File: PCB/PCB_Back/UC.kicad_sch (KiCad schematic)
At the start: 39 parts, among them J1 Sensor connector, J2 USB_C_Receptacle_USB2.0, J3 Lipo connector, Q1 UMH3N, Q2 PMOS, SW1 SW_Push_Dual, U1 ESP-12E, U2 CH340C, U3 MCP73831-2-OT, U4 MCP1700x-330xxTT, U6 BME680

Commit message: Layout, Routing, Stuff
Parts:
- removed H4, H5: MountingHole, MountingHole:MountingHole_2.7mm_M2.5, symbol Mechanical:MountingHole
- added C24, C25: 100nF, Capacitor_SMD:C_0805_2012Metric, symbol Device:C
- R9: footprint Resistor_SMD:R_0815_2038Metric -> Resistor_SMD:R_0805_2012Metric
- U6: footprint KH-6X6X6H-STM:KH-6X6X6H-STM -> Package_LGA:Bosch_LGA-8_3x3mm_P0.8mm_ClockwisePinNumbering
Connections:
- net +3V3: now also C24.1, C25.1
- net GND: now also C24.2, C25.2
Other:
- company: (none) -> Waldo
- title: (none) -> Blahaj_Back

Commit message: Misc. Fixes, v1.0.
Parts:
- removed Q2: PMOS, Package_TO_SOT_SMD:SOT-23, symbol Simulation_SPICE:PMOS
- added Q3: Q_PMOS_GSD, Package_TO_SOT_SMD:SOT-23, symbol Device:Q_PMOS_GSD
- added SW2: SW_PWR, easyeda2kicad:SW-SMD_MK-12C02-G025, symbol Switch:SW_SPDT
- D16: footprint LED_SMD:LED_0805_2012Metric -> LED_SMD:LED_1206_3216Metric
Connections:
- net +5V: now also Q3.1 (G)
- net +BATT: now also Q3.3 (D)
- net VCC: now also SW2.2 (B); no longer C20.1, D17.1 (K)
- new net: C20.1, D17.1 (K), Q3.2 (S), SW2.3 (C)
- no-connect marks 17 -> 18
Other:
- moved on the sheet: C19, C20, D17, R13, U4

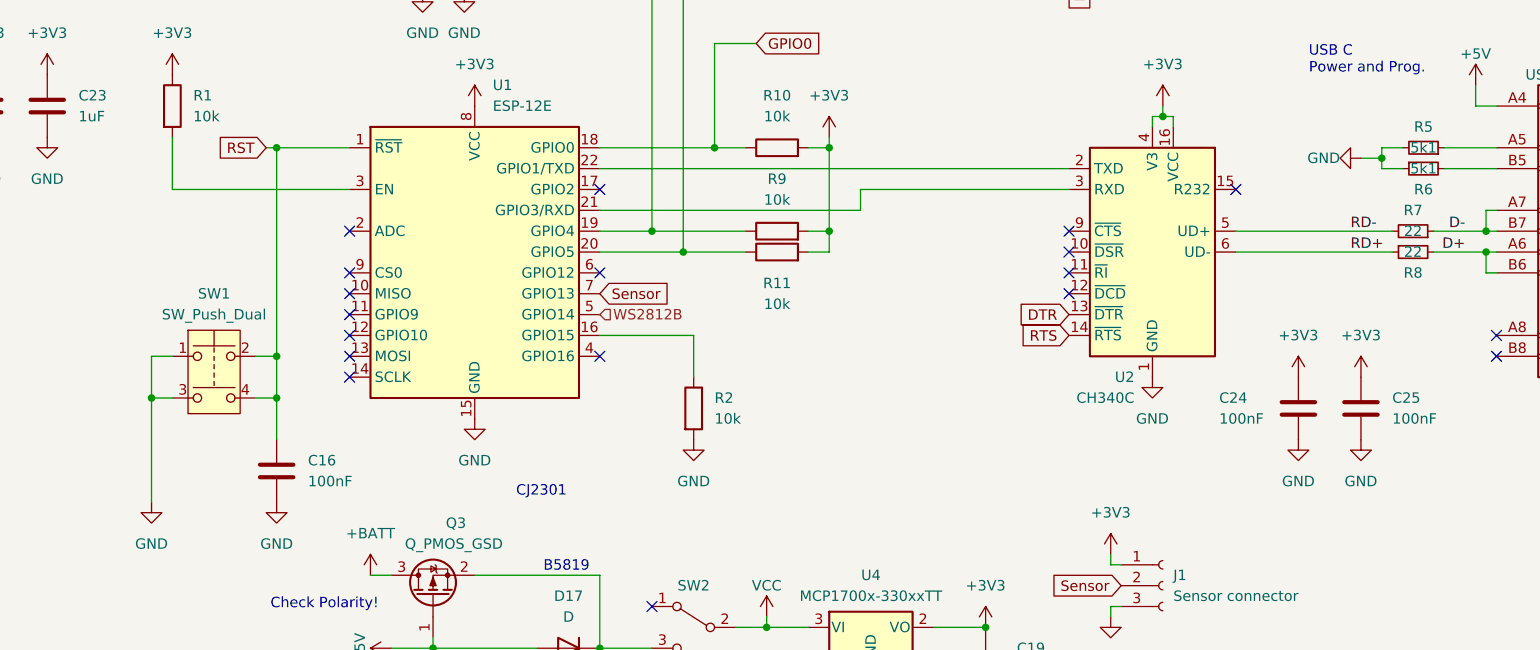
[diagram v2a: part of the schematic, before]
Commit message: Switched D+/D-, TX/RX, Switch Pins and rotated Lipo Marking
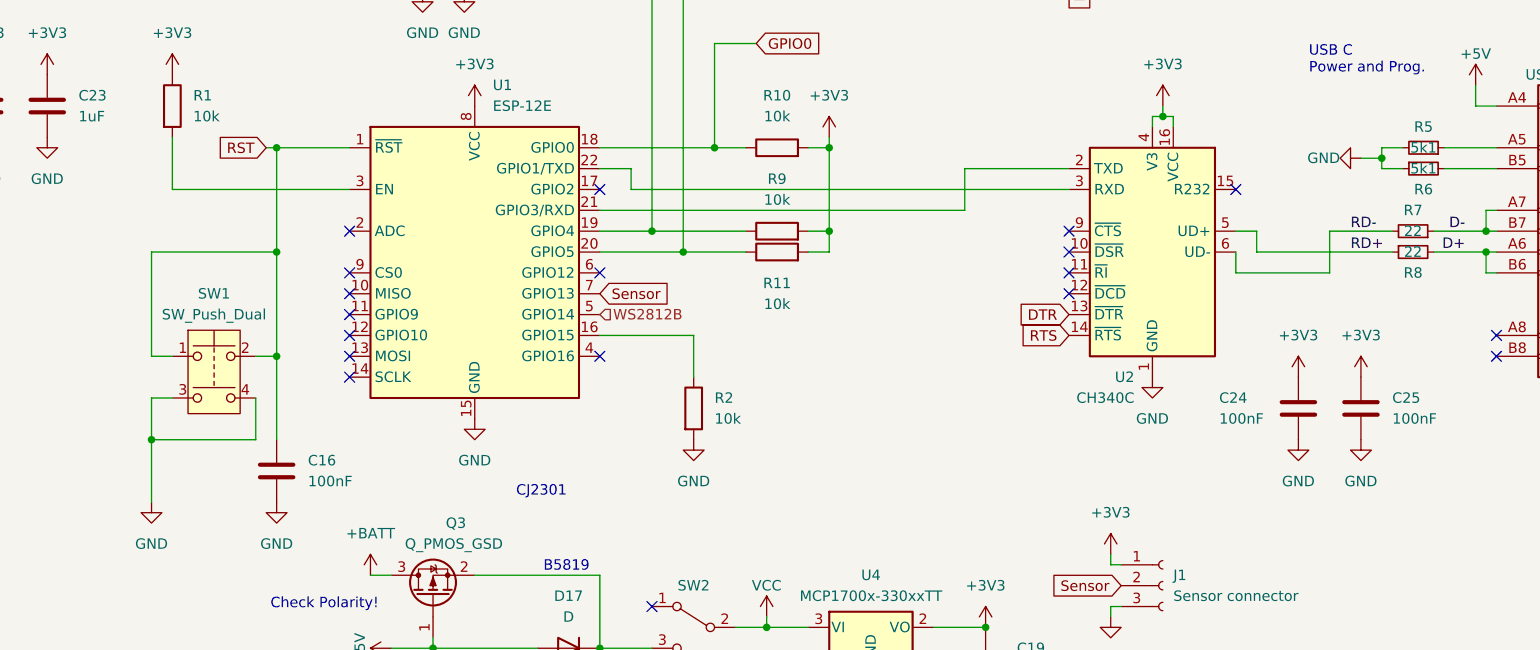
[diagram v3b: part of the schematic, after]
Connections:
- net GND: now also SW1.4; no longer SW1.1
- net RD+: now also U2.5 (UD+); no longer U2.6 (UD-)
- net RD-: now also U2.6 (UD-); no longer U2.5 (UD+)
- net RST: now also SW1.1; no longer SW1.4
- net at U1.21 (GPIO3/RXD): now also U2.2 (TXD); no longer U2.3 (RXD)
- net at U1.22 (GPIO1/TXD): now also U2.3 (RXD); no longer U2.2 (TXD)
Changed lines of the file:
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@@
-	)
-	(junction
-		(at 92.71 111.76)
-		(diameter 0)
-		(color 0 0 0 0)
-	)
-	(junction
-		(at 77.47 111.76)
-		(diameter 0)
-		(color 0 0 0 0)
 	)
 	(junction
@@
 	)
 	(junction
+		(at 77.47 116.84)
+		(diameter 0)
+		(color 0 0 0 0)
+	)
+	(junction
 		(at 256.54 115.57)
 		(diameter 0)
@@
 	)
 	(junction
+		(at 92.71 93.98)
+		(diameter 0)
+		(color 0 0 0 0)
+	)
+	(junction
 		(at 111.76 142.24)
 		(diameter 0)
@@
 	(wire
 		(pts
-			(xy 92.71 81.28) (xy 92.71 106.68)
+			(xy 92.71 81.28) (xy 92.71 93.98)
 		)
 		(stroke
@@
 	(wire
 		(pts
+			(xy 135.89 83.82) (xy 132.08 83.82)
+		)
+		(stroke
+			(width 0)
+			(type default)
+		)
+	)
+	(wire
+		(pts
 			(xy 143.51 104.14) (xy 132.08 104.14)
 		)
@@
 	(wire
 		(pts
+			(xy 189.23 86.36) (xy 135.89 86.36)
+		)
+		(stroke
+			(width 0)
+			(type default)
+		)
+	)
+	(wire
+		(pts
 			(xy 128.27 54.61) (xy 146.05 54.61)
 		)
@@
 	(wire
 		(pts
+			(xy 92.71 93.98) (xy 92.71 106.68)
+		)
+		(stroke
+			(width 0)
+			(type default)
+		)
+	)
+	(wire
+		(pts
+			(xy 209.55 93.98) (xy 209.55 96.52)
+		)
+		(stroke
+			(width 0)
+			(type default)
+		)
+	)
+	(wire
+		(pts
 			(xy 69.85 173.99) (xy 71.12 173.99)
 		)
@@
 	(wire
 		(pts
+			(xy 135.89 86.36) (xy 135.89 83.82)
+		)
+		(stroke
+			(width 0)
+			(type default)
+		)
+	)
+	(wire
+		(pts
 			(xy 160.02 91.44) (xy 160.02 93.98)
 		)
@@
 	(wire
 		(pts
-			(xy 163.83 86.36) (xy 189.23 86.36)
-		)
-		(stroke
-			(width 0)
-			(type default)
-		)
-	)
-	(wire
-		(pts
 			(xy 80.01 86.36) (xy 101.6 86.36)
 		)
@@
 	(wire
 		(pts
-			(xy 132.08 88.9) (xy 163.83 88.9)
+			(xy 189.23 83.82) (xy 176.53 83.82)
 		)
 		(stroke
@@
 	(wire
 		(pts
-			(xy 132.08 83.82) (xy 189.23 83.82)
-		)
-		(stroke
-			(width 0)
-			(type default)
-		)
-	)
-	(wire
-		(pts
 			(xy 240.03 93.98) (xy 240.03 96.52)
 		)
@@
 	(wire
 		(pts
+			(xy 212.09 91.44) (xy 209.55 91.44)
+		)
+		(stroke
+			(width 0)
+			(type default)
+		)
+	)
+	(wire
+		(pts
 			(xy 142.24 44.45) (xy 142.24 93.98)
 		)
@@
 	(wire
 		(pts
+			(xy 176.53 88.9) (xy 132.08 88.9)
+		)
+		(stroke
+			(width 0)
+			(type default)
+		)
+	)
+	(wire
+		(pts
 			(xy 50.8 146.05) (xy 50.8 147.32)
 		)
@@
 	(wire
 		(pts
-			(xy 77.47 111.76) (xy 77.47 124.46)
-		)
-		(stroke
-			(width 0)
-			(type default)
-		)
-	)
-	(wire
-		(pts
-			(xy 90.17 111.76) (xy 92.71 111.76)
+			(xy 77.47 111.76) (xy 77.47 116.84)
 		)
 		(stroke
@@
 	(wire
 		(pts
+			(xy 77.47 93.98) (xy 77.47 106.68)
+		)
+		(stroke
+			(width 0)
+			(type default)
+		)
+	)
+	(wire
+		(pts
+			(xy 228.6 91.44) (xy 220.98 91.44)
+		)
+		(stroke
+			(width 0)
+			(type default)
+		)
+	)
+	(wire
+		(pts
 			(xy 227.33 82.55) (xy 224.79 82.55)
 		)
@@
 	(wire
 		(pts
-			(xy 92.71 106.68) (xy 92.71 111.76)
+			(xy 90.17 111.76) (xy 90.17 116.84)
+		)
+		(stroke
+			(width 0)
+			(type default)
+		)
+	)
+	(wire
+		(pts
+			(xy 77.47 116.84) (xy 77.47 124.46)
 		)
 		(stroke
@@
 	(wire
 		(pts
+			(xy 92.71 93.98) (xy 77.47 93.98)
+		)
+		(stroke
+			(width 0)
+			(type default)
+		)
+	)
+	(wire
+		(pts
 			(xy 240.03 88.9) (xy 240.03 91.44)
 		)
@@
 	(wire
 		(pts
-			(xy 209.55 93.98) (xy 228.6 93.98)
-		)
-		(stroke
-			(width 0)
-			(type default)
-		)
-	)
-	(wire
-		(pts
 			(xy 172.72 139.7) (xy 179.07 139.7)
 		)
@@
 	(wire
 		(pts
-			(xy 77.47 106.68) (xy 77.47 111.76)
-		)
-		(stroke
-			(width 0)
-			(type default)
-		)
-	)
-	(wire
-		(pts
 			(xy 194.31 138.43) (xy 194.31 137.16)
 		)
@@
 	(wire
 		(pts
+			(xy 220.98 96.52) (xy 209.55 96.52)
+		)
+		(stroke
+			(width 0)
+			(type default)
+		)
+	)
+	(wire
+		(pts
 			(xy 132.08 91.44) (xy 138.43 91.44)
 		)
@@
 	(wire
 		(pts
+			(xy 176.53 83.82) (xy 176.53 88.9)
+		)
+		(stroke
+			(width 0)
+			(type default)
+		)
+	)
+	(wire
+		(pts
 			(xy 146.05 81.28) (xy 146.05 68.58)
 		)
@@
 	(wire
 		(pts
+			(xy 220.98 91.44) (xy 220.98 96.52)
+		)
+		(stroke
+			(width 0)
+			(type default)
+		)
+	)
+	(wire
+		(pts
 			(xy 132.08 133.35) (xy 132.08 142.24)
 		)
@@
 	(wire
 		(pts
+			(xy 90.17 116.84) (xy 77.47 116.84)
+		)
+		(stroke
+			(width 0)
+			(type default)
+		)
+	)
+	(wire
+		(pts
 			(xy 227.33 82.55) (xy 227.33 83.82)
 		)
@@
 	(wire
 		(pts
-			(xy 163.83 88.9) (xy 163.83 86.36)
-		)
-		(stroke
-			(width 0)
-			(type default)
-		)
-	)
-	(wire
-		(pts
-			(xy 92.71 111.76) (xy 92.71 116.84)
+			(xy 92.71 106.68) (xy 92.71 116.84)
 		)
 		(stroke
@@
 	(wire
 		(pts
-			(xy 209.55 91.44) (xy 228.6 91.44)
-		)
-		(stroke
-			(width 0)
-			(type default)
-		)
-	)
-	(wire
-		(pts
 			(xy 104.14 133.35) (xy 106.68 133.35)
 		)
@@
 	(wire
 		(pts
+			(xy 228.6 93.98) (xy 212.09 93.98)
+		)
+		(stroke
+			(width 0)
+			(type default)
+		)
+	)
+	(wire
+		(pts
 			(xy 229.87 83.82) (xy 227.33 83.82)
 		)
@@
 		)
 		(stroke
+			(width 0)
+			(type default)
+		)
+	)
+	(wire
+		(pts
+			(xy 212.09 93.98) (xy 212.09 91.44)
+		)
+		(stroke

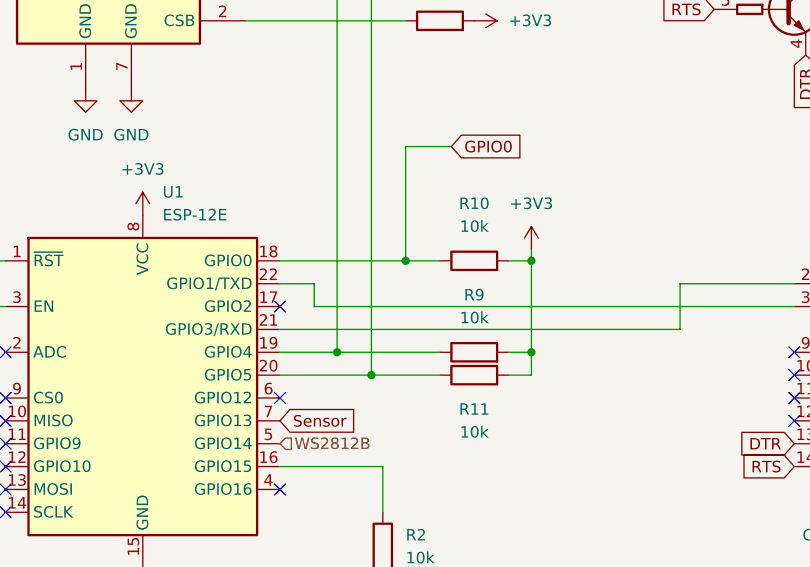
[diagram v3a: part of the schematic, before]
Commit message: Added R14 10k Pullup to GPIO2
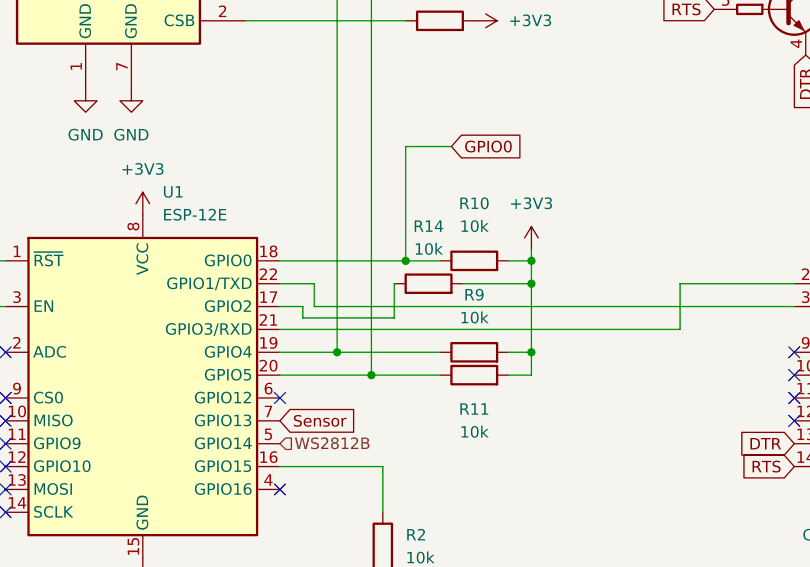
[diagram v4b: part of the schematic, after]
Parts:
- added R14: 10k, Resistor_SMD:R_0805_2012Metric, symbol Device:R
- D17: footprint Diode_SMD:D_SOD-323 -> Diode_SMD:D_SOD-323_HandSoldering
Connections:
- net +3V3: now also R14.2
- net at U1.17 (GPIO2): now also R14.1
- no-connect marks 18 -> 17
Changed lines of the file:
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@@
 	)
 	(junction
+		(at 160.02 83.82)
+		(diameter 0)
+		(color 0 0 0 0)
+	)
+	(junction
 		(at 160.02 91.44)
 		(diameter 0)
@@
 	)
 	(no_connect
-		(at 132.08 86.36)
-	)
-	(no_connect
 		(at 101.6 96.52)
 	)
@@
 	(wire
 		(pts
+			(xy 160.02 83.82) (xy 160.02 91.44)
+		)
+		(stroke
+			(width 0)
+			(type default)
+		)
+	)
+	(wire
+		(pts
 			(xy 240.03 93.98) (xy 233.68 93.98)
 		)
@@
 	(wire
 		(pts
+			(xy 134.62 87.63) (xy 144.78 87.63)
+		)
+		(stroke
+			(width 0)
+			(type default)
+		)
+	)
+	(wire
+		(pts
 			(xy 152.4 138.43) (xy 152.4 139.7)
 		)
@@
 	(wire
 		(pts
-			(xy 160.02 81.28) (xy 160.02 91.44)
+			(xy 160.02 81.28) (xy 160.02 83.82)
 		)
 		(stroke
@@
 	(wire
 		(pts
+			(xy 152.4 83.82) (xy 160.02 83.82)
+		)
+		(stroke
+			(width 0)
+			(type default)
+		)
+	)
+	(wire
+		(pts
 			(xy 229.87 81.28) (xy 227.33 81.28)
 		)
@@
 	(wire
 		(pts
+			(xy 134.62 86.36) (xy 134.62 87.63)
+		)
+		(stroke
+			(width 0)
+			(type default)
+		)
+	)
+	(wire
+		(pts
 			(xy 104.14 133.35) (xy 106.68 133.35)
 		)
@@
 	(wire
 		(pts
+			(xy 144.78 87.63) (xy 144.78 83.82)
+		)
+		(stroke
+			(width 0)
+			(type default)
+		)
+	)
+	(wire
+		(pts
+			(xy 132.08 86.36) (xy 134.62 86.36)
+		)
+		(stroke
+			(width 0)
+			(type default)
+		)
+	)
+	(wire
+		(pts
 			(xy 26.67 152.4) (xy 29.21 152.4)
 		)
@@
 			)
 		)
-		(property "Footprint" "Diode_SMD:D_SOD-323"
+		(property "Footprint" "Diode_SMD:D_SOD-323_HandSoldering"
 			(at 128.27 142.24 0)
 			(effects
@@
 					(unit 1)
 				)
+			)
+		)
+	)
+	(symbol
+		(lib_id "Device:R")
+		(at 148.59 83.82 90)
+		(unit 1)
+		(exclude_from_sim no)
+		(in_bom yes)
+		(on_board yes)
+		(dnp no)
+		(fields_autoplaced yes)
+		(property "Reference" "R14"
+			(at 148.59 77.47 90)
+			(effects
+				(font
+					(size 1.27 1.27)
+				)
+			)
+		)
+		(property "Value" "10k"
+			(at 148.59 80.01 90)
+			(effects
+				(font
+					(size 1.27 1.27)
+				)
+			)
+		)
+		(property "Footprint" "Resistor_SMD:R_0805_2012Metric"
+			(at 148.59 85.598 90)
+			(effects
+				(font
+					(size 1.27 1.27)
+				)
+				(hide yes)
+			)
+		)
+		(property "Datasheet" "~"
+			(at 148.59 83.82 0)
+			(effects
+				(font
+					(size 1.27 1.27)
+				)
+				(hide yes)
+			)
+		)
+		(property "Description" "Resistor"
+			(at 148.59 83.82 0)
+			(effects
+				(font
+					(size 1.27 1.27)
+				)
+				(hide yes)
+			)
+		)
+		(pin "1"
+		)
+		(pin "2"
+		)
+		(instances
+			(project ""
+				(path "/a7f720df-5226-47da-b97d-a699f8341512/1b10c049-f943-40db-a187-9221f68b2962"
+					(reference "R14")
+					(unit 1)
+				)

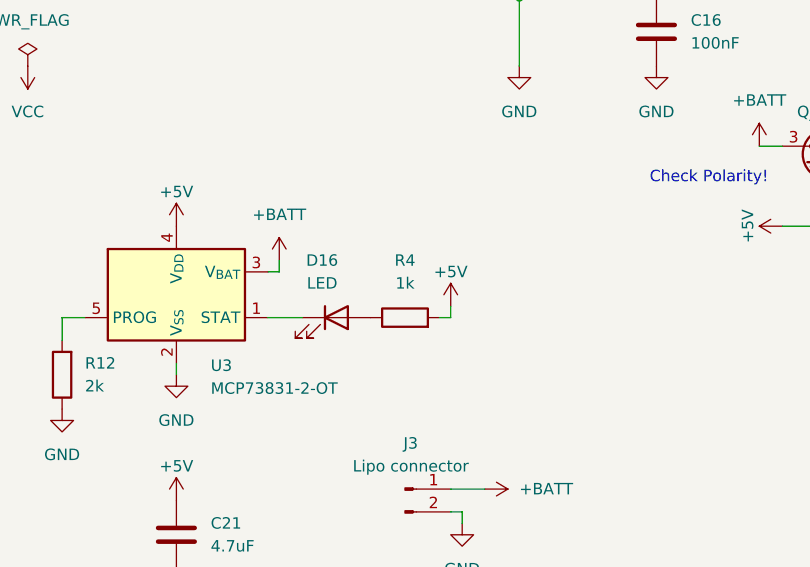
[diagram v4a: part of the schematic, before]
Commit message: Switched D16 Resistor from 1k to 2k
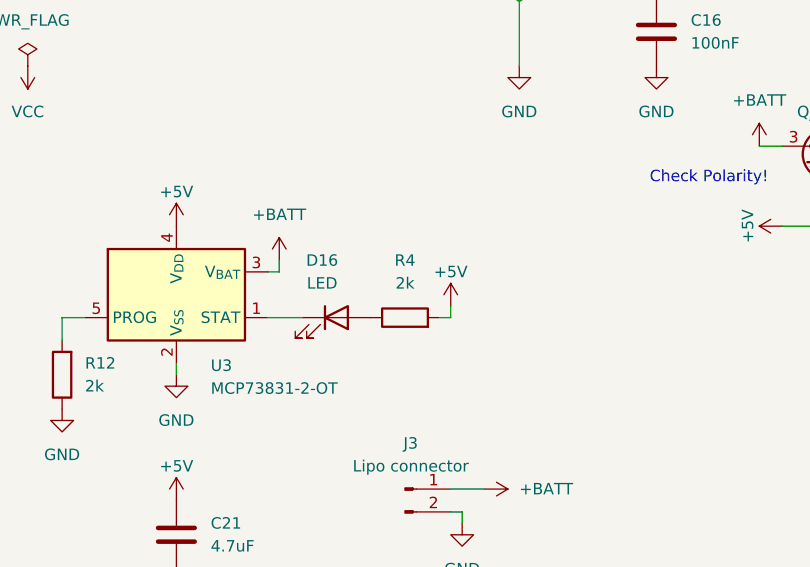
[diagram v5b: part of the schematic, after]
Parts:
- R4: value 1k -> 2k
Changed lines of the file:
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@@
 			)
 		)
-		(property "Value" "1k"
+		(property "Value" "2k"
 			(at 64.77 148.59 90)
 			(effects

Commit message: Change J1 to SMD, Production
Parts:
- J1: footprint Connector_PinSocket_2.54mm:PinSocket_1x03_P2.54mm_Horizontal -> easyeda2kicad:HDR-SMD_3P-P2.54-H-F-L11.5
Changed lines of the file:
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@@
 			)
 		)
-		(property "Footprint" "Connector_PinSocket_2.54mm:PinSocket_1x03_P2.54mm_Horizontal"
+		(property "Footprint" "easyeda2kicad:HDR-SMD_3P-P2.54-H-F-L11.5"
 			(at 200.66 134.62 0)
 			(effects
